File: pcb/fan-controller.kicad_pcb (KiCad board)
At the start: 2 copper layers, 52 x 58.1 mm, 30 parts, among them J1 Barrel_Jack, J2 Conn_01x04_Pin, J3 Conn_01x04_Pin, J4 Conn_01x04_Pin, J5 Conn_01x04_Pin, J6 Conn_01x04_Pin, J7 Conn_01x04_Pin, Q1 2N7002, U2 AMS1117-5.0, U3 SHT4x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

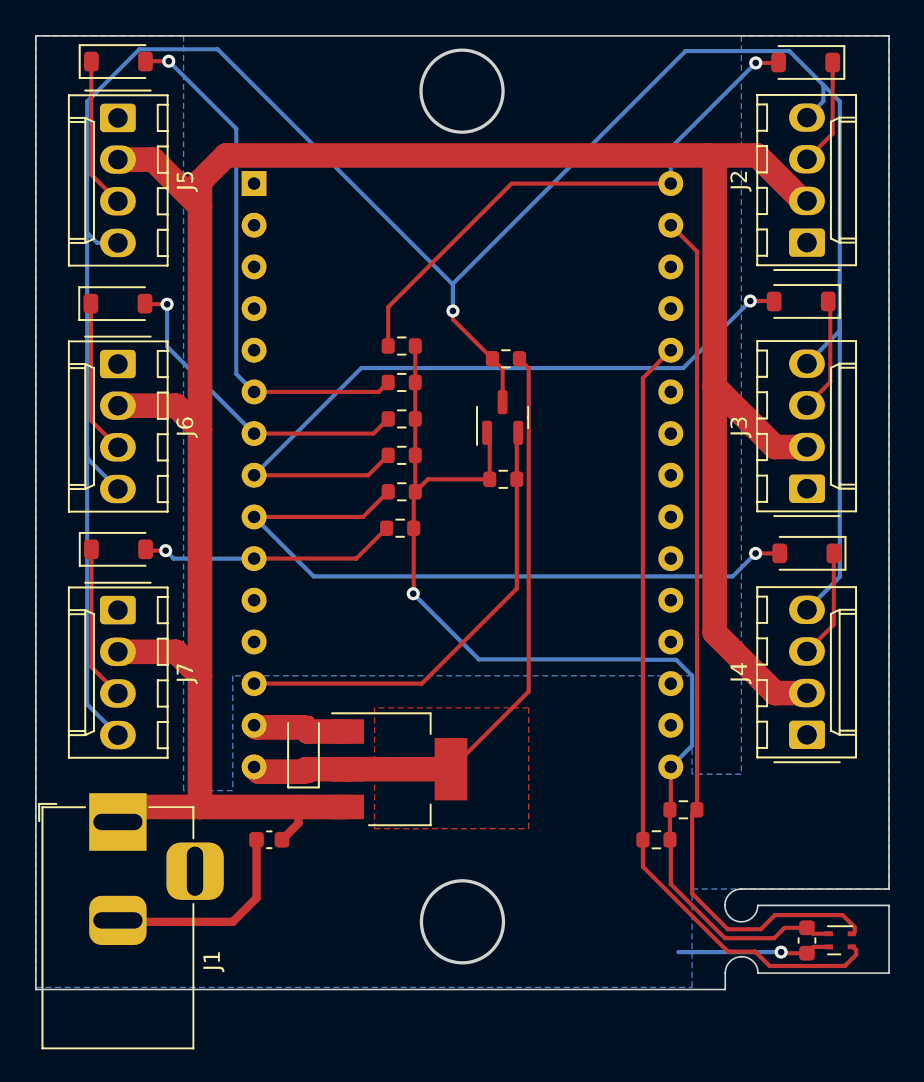
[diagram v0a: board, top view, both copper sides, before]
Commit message: change voltage regulation
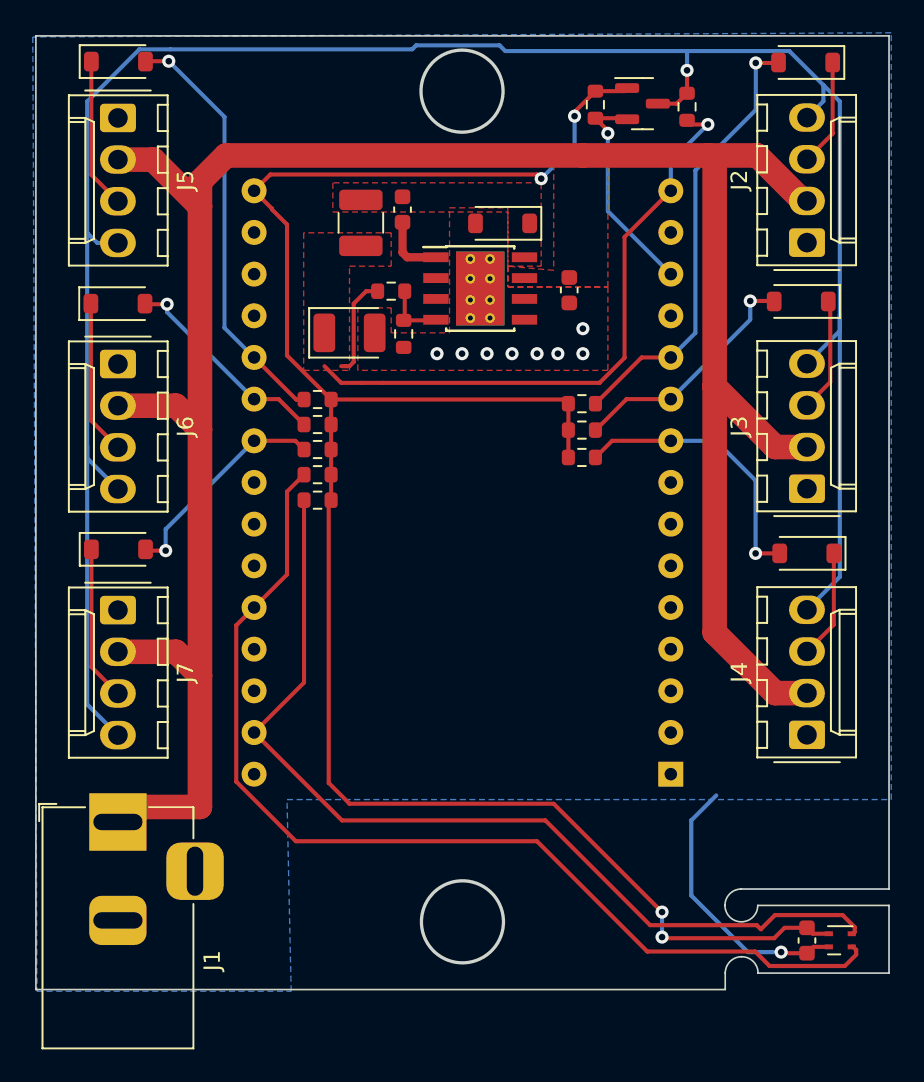
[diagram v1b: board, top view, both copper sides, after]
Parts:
- removed U2: AMS1117-5.0, Package_TO_SOT_SMD:SOT-223-3_TabPin2
- added C2: 10uF, Capacitor_SMD:C_0603_1608Metric, F.Cu at (52.5, 35.5)
- added D7: D_Schottky, Diode_SMD:D_SOD-123, F.Cu at (48.4, 31.4)
- added L1: 15uH, Inductor_SMD:L_1210_3225Metric, F.Cu at (39.8, 31.4)
- added R11: 10K, Resistor_SMD:R_0603_1608Metric, F.Cu at (41.7, 35.6)
- added R12: 3.24K, Resistor_SMD:R_0603_1608Metric, F.Cu at (42.4, 38.2)
- added U1: TPS5430DDA, Package_SO:TI_SO-PowerPAD-8_ThermalVias, F.Cu at (47.1, 35.4)
- C3: value 10uF -> 0.01uF
- C4: value 10uF -> 220uF; footprint Capacitor_Tantalum_SMD:CP_EIA-3216-18_Kemet-A -> Capacitor_Tantalum_SMD:CP_EIA-3528-12_Kemet-T
- moved C3 39.3 mm to (42.3, 30.6), turned to 90 degrees
- moved U4 36.0 mm to (46.0, 65.0), turned to 180 degrees
- moved R4 30.4 mm to (37.2, 46.7)
- moved R5 29.2 mm to (37.2, 48.3), turned to 0 degrees
- moved C4 25.6 mm to (39.1, 38.1), turned to 0 degrees
- moved R3 23.5 mm to (54.1, 24.2), turned to 90 degrees
- moved Q1 20.9 mm to (57.0, 24.1), turned to 0 degrees
- moved R2 18.9 mm to (59.7, 24.3), turned to -90 degrees
- moved R1 11.5 mm to (53.3, 42.4), turned to 180 degrees
- moved R7 11.2 mm to (53.3, 45.7), turned to 180 degrees
- moved R6 11.1 mm to (53.3, 44.0), turned to 180 degrees
- moved R10 6.95 mm to (37.2, 45.2)
- moved R8 5.23 mm to (37.2, 42.2)
- moved R9 5.14 mm to (37.2, 43.7)
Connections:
- C3 pad 1: +12V -> Net-(U1-BOOT)
- C3 pad 2: GND -> Net-(D7-K)
- U4 pad 10: TACO_6 -> TACO_2
- U4 pad 11: unconnected-(U4-IO14-Pad11) -> TACO_1
- U4 pad 20: unconnected-(U4-IO4-Pad20) -> TACO_4
- U4 pad 21: unconnected-(U4-IO16-Pad21) -> TACO_5
- U4 pad 22: unconnected-(U4-IO17-Pad22) -> TACO_6
- U4 pad 30: TACO_1 -> unconnected-(U4-IO23-Pad30)
- U4 pad 6: TACO_4 -> unconnected-(U4-IO32-Pad6)
- U4 pad 7: TACO_5 -> unconnected-(U4-IO33-Pad7)
- U4 pad 8: TACO_2 -> unconnected-(U4-IO25-Pad8)
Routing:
- net +3.3V: track 66.7 -> 118.4 mm, vias 1 -> 4
- net TACO_2: track 44.8 -> 14.8 mm
- net TACO_3: track 42.9 -> 17.1 mm
- net PWM_OUT: track 153.3 -> 136.3 mm
- net SDA: track 48.6 -> 63.8 mm
- net PWM_1: track 27.9 -> 13.4 mm, vias 0 -> 1
- net +12V: track 154.7 -> 143.2 mm
- net GND: track 27.9 -> 16.7 mm, vias 1 -> 9
- net TACO_5: track 20.0 -> 13.0 mm
- net TACO_4: track 32.2 -> 25.7 mm
- net TACO_1: track 33.6 -> 27.3 mm
- net SCL: track 53.5 -> 58.2 mm
- net Net-(U1-BOOT): track 0.00 -> 4.00 mm
- net +5V: track 39.4 -> 43.2 mm, vias 0 -> 1
- net Net-(U1-VSENSE): track 0.00 -> 3.78 mm
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- added copper zone on F.Cu, net +12V
- added copper zone on F.Cu, net GND
- added copper zone on F.Cu, net Net-(D7-K)
